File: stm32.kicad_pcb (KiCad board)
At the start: 4 copper layers, 50 x 100 mm, 108 parts, among them CN1 SM04B-SRSS-TB (LF)(SN), J3 B2B-PH-SM4-TB (LF)(SN), P1 TYPE-C 16PIN 2MD(073), Q1 DMG2301L-7, SW1 JS102011JCQN, U1 STM32L431KBU6_C2826408, U13 CH340C_C7464026, U2 MCP73833T-AMI/MF, U3 TPS631000DRLR, U4 OPT3004DNPR, U5 XC6206P332MR_C347376, U6 INA260AIPWR, U8 BME280

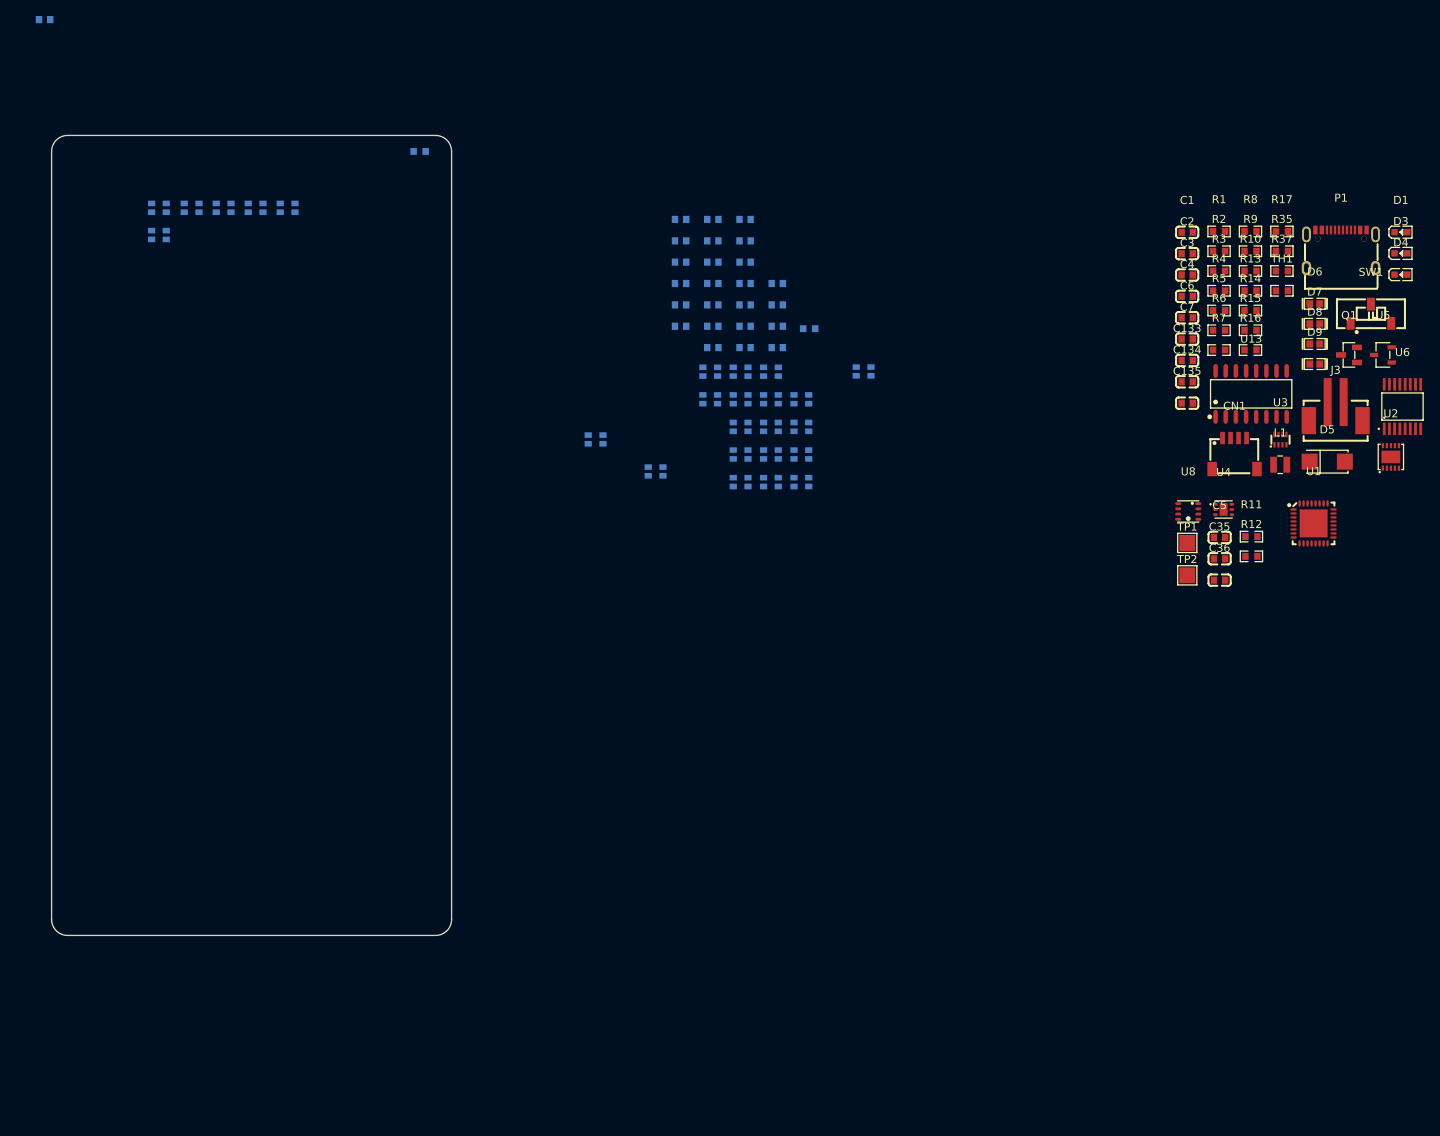
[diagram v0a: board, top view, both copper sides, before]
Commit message: Added pull up / pull down on mode pin tps
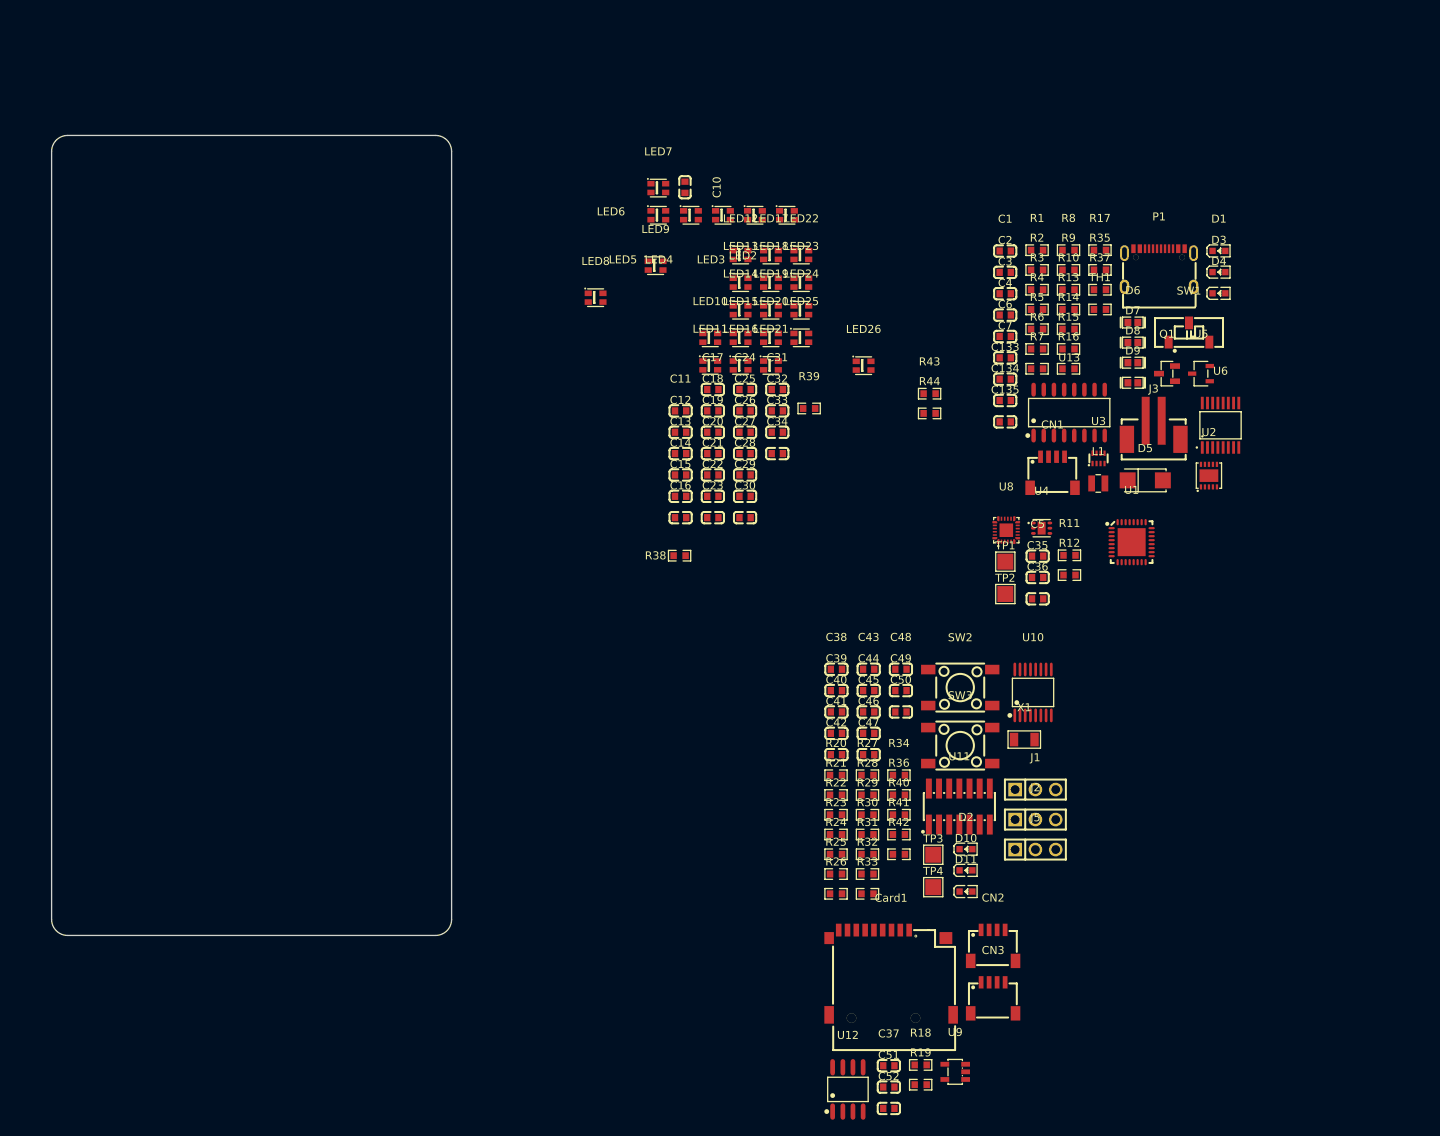
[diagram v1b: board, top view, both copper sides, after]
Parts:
- added C37: CC0603KRX7R9BB104, easyeda2kicad:C0603, F.Cu at (154.2, 150.3)
- added C38: CL10A475KO8NNNC, easyeda2kicad:C0603, F.Cu at (147.6, 100.7)
- added C39: CC0603KRX7R9BB104, easyeda2kicad:C0603, F.Cu at (147.6, 103.4)
- added C40: CC0603KRX7R9BB104, easyeda2kicad:C0603, F.Cu at (147.6, 106.1)
- added C41: CC0603KRX7R9BB104, easyeda2kicad:C0603, F.Cu at (147.6, 108.7)
- added C42: CL10A105KB8NNNC, easyeda2kicad:C0603, F.Cu at (147.6, 111.4)
- added C43: CL10A105KB8NNNC, easyeda2kicad:C0603, F.Cu at (151.6, 100.7)
- added C44: 0603CG7R0C500NT, easyeda2kicad:C0603, F.Cu at (151.6, 103.4)
- added C45: 0603CG7R0C500NT, easyeda2kicad:C0603, F.Cu at (151.6, 106.1)
- added C46: CC0603KRX7R9BB104, easyeda2kicad:C0603, F.Cu at (151.6, 108.7)
- added C47: CC0603KRX7R9BB104, easyeda2kicad:C0603, F.Cu at (151.6, 111.4)
- added C48: CC0603KRX7R9BB104, easyeda2kicad:C0603, F.Cu at (155.7, 100.7)
- added C49: CC0603KRX7R9BB104, easyeda2kicad:C0603, F.Cu at (155.7, 103.4)
- added C50: CC0603KRX7R9BB104, easyeda2kicad:C0603, F.Cu at (155.7, 106.1)
- added C51: CC0603KRX7R9BB104, easyeda2kicad:C0603, F.Cu at (154.2, 153.0)
- added C52: CC0603KRX7R9BB104, easyeda2kicad:C0603, F.Cu at (154.2, 155.6)
- added CN2: SM04B-SRSS-TB (LF)(SN), easyeda2kicad:CONN-SMD_4P-P1.00_SM04B-SRSS-TB-LF-SN, F.Cu at (167.2, 135.2)
- added CN3: SM04B-SRSS-TB (LF)(SN), easyeda2kicad:CONN-SMD_4P-P1.00_SM04B-SRSS-TB-LF-SN, F.Cu at (167.2, 141.8)
- added Card1: TF PUSH, easyeda2kicad:TF-SMD_TF-PUSH, F.Cu at (154.4, 138.6)
- added D10: KT-0603R, easyeda2kicad:LED0603-RD, F.Cu at (163.8, 125.9)
- added D11: KT-0603R, easyeda2kicad:LED0603-RD, F.Cu at (163.8, 128.5)
- added D2: 0603 Green 509-620mcd, easyeda2kicad:LED0603-RD, F.Cu at (163.8, 123.2)
- added J1: PZ254V-11-03P_C2937625, easyeda2kicad:HDR-TH_3P-P2.54-V-M, F.Cu at (172.5, 115.8)
- added J2: PZ254V-11-03P_C2937625, easyeda2kicad:HDR-TH_3P-P2.54-V-M, F.Cu at (172.5, 119.5)
- added J5: PZ254V-11-03P_C2937625, easyeda2kicad:HDR-TH_3P-P2.54-V-M, F.Cu at (172.5, 123.3)
- added R18: 0603WAF1002T5E, easyeda2kicad:R0603, F.Cu at (158.1, 150.2)
- added R19: 0603WAF1002T5E, easyeda2kicad:R0603, F.Cu at (158.1, 152.7)
- added R20: 0603WAF4701T5E, easyeda2kicad:R0603, F.Cu at (147.6, 114.0)
- added R21: 0603WAF1002T5E, easyeda2kicad:R0603, F.Cu at (147.6, 116.4)
- added R22: 0603WAF1000T5E, easyeda2kicad:R0603, F.Cu at (147.6, 118.9)
- added R23: 0603WAF1000T5E, easyeda2kicad:R0603, F.Cu at (147.6, 121.4)
- added R24: 0603WAF1000T5E, easyeda2kicad:R0603, F.Cu at (147.6, 123.9)
- added R25: 0603WAF220JT5E, easyeda2kicad:R0603, F.Cu at (147.6, 126.3)
- added R26: 0603WAF0000T5E, easyeda2kicad:R0603, F.Cu at (147.6, 128.8)
- added R27: 0603WAF0000T5E, easyeda2kicad:R0603, F.Cu at (151.5, 114.0)
- added R28: 0603WAF0000T5E, easyeda2kicad:R0603, F.Cu at (151.5, 116.4)
- added R29: 0603WAF0000T5E, easyeda2kicad:R0603, F.Cu at (151.5, 118.9)
- added R30: 0603WAF1002T5E, easyeda2kicad:R0603, F.Cu at (151.5, 121.4)
- added R31: 0603WAF1002T5E, easyeda2kicad:R0603, F.Cu at (151.5, 123.9)
- added R32: 0603WAF220JT5E, easyeda2kicad:R0603, F.Cu at (151.5, 126.3)
- added R33: 0603WAF220JT5E, easyeda2kicad:R0603, F.Cu at (151.5, 128.8)
- added R34: 0603WAF4701T5E, easyeda2kicad:R0603, F.Cu at (155.4, 114.0)
- added R36: 0603WAF1002T5E, easyeda2kicad:R0603, F.Cu at (155.4, 116.4)
- added R40: 0603WAF4701T5E, easyeda2kicad:R0603, F.Cu at (155.4, 118.9)
- added R41: 0603WAF1001T5E, easyeda2kicad:R0603, F.Cu at (155.4, 121.4)
- added R42: 0603WAF1000T5E, easyeda2kicad:R0603, F.Cu at (155.4, 123.9)
- added R43: 0603WAF1002T5E, easyeda2kicad:R0603, F.Cu at (159.2, 66.3)
- added R44: 0603WAF1002T5E, easyeda2kicad:R0603, F.Cu at (159.2, 68.8)
- added SW2: 6.0*6.0*6.0, easyeda2kicad:SW-SMD_4P-L6.0-W6.0-P4.50-LS8.6, F.Cu at (163.1, 103.0)
- added SW3: 6.0*6.0*6.0, easyeda2kicad:SW-SMD_4P-L6.0-W6.0-P4.50-LS8.6, F.Cu at (163.1, 110.3)
- added TP3: TestPoint, TestPoint:TestPoint_Pad_2.0x2.0mm, F.Cu at (159.7, 123.9)
- added TP4: TestPoint, TestPoint:TestPoint_Pad_2.0x2.0mm, F.Cu at (159.7, 128.0)
- added U10: MAX3221ECPWR, easyeda2kicad:TSSOP-16_L5.0-W4.4-P0.65-LS6.4-BL, F.Cu at (172.2, 103.6)
- added U11: HB-PH9-12727PB2GOB, easyeda2kicad:HDR-SMD_14P-P1.27-V-M-R2-C7-LS5.5, F.Cu at (163.0, 117.9)
- added U12: TMP75AIDR, easyeda2kicad:SOIC-8_L4.9-W3.9-P1.27-LS6.0-BL, F.Cu at (149.0, 153.2)
- added U9: SN74AHCT1G125DBVR, easyeda2kicad:SOT-23-5_L3.0-W1.7-P0.95-LS2.8-BR, F.Cu at (162.4, 151.1)
- added X1: SC-32S32.768kHz20PPM7pF, easyeda2kicad:OSC-SMD_L3.2-W1.5, F.Cu at (171.1, 109.5)
- C10, C11, C12, C13, C14, C15, C16, C17, C18, C19, C20, C21, C22, C23, C24, C25, C26, C27, C28, C29, C30, C31, C32, C33, C34, LED10, LED11, LED12, LED13, LED14, LED15, LED16, LED17, LED18, LED19, LED2, LED20, LED21, LED22, LED23, LED24, LED25, LED26, LED3, LED4, LED5, LED6, LED7, LED8, LED9, R38, R39: moved to F.Cu
- U8: value BME280 -> MPU6500; footprint easyeda2kicad:LGA-8_BME280_BL -> easyeda2kicad:QFN-24_L3.0-W3.0-P0.40-BL-EP
- moved C10 82.7 mm to (128.7, 40.5), turned to -90 degrees
- moved LED7 62.7 mm to (125.3, 40.6)
- moved LED6 62.4 mm to (125.3, 44.0)
- moved LED2 62.4 mm to (141.4, 44.0)
- moved LED3 62.4 mm to (137.4, 44.0)
- moved LED4 62.4 mm to (133.4, 44.0)
- moved LED5 62.4 mm to (129.4, 44.0)
- moved R38 60.1 mm to (128.0, 86.5)
- moved C16 37.3 mm to (128.1, 81.8)
- moved C23 37.3 mm to (132.2, 81.8)
- moved C30 37.3 mm to (136.2, 81.8)
- moved C15 31.9 mm to (128.1, 79.1)
- moved C22 31.9 mm to (132.2, 79.1)
- moved C29 31.9 mm to (136.2, 79.1)
- moved LED12 28.4 mm to (135.6, 48.9)
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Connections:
- net /USB/scl2 renamed /stm32_page/I2C3_SCL
- net /sensors/DIN renamed /sensors/led_matrix/DIN
- CN1 pad 3: /USB/sda2 -> /stm32_page/I2C3_SDA
- R17 pad 1: /USB/sda2 -> /stm32_page/I2C3_SDA
- U1 pad 1: unconnected-(U1-VDD-Pad1) -> +3V3
- U1 pad 10: unconnected-(U1-PA4-Pad10) -> /stm32_page/SD_CD
- U1 pad 11: unconnected-(U1-PA5-Pad11) -> /stm32_page/IMU_INT
- U1 pad 12: unconnected-(U1-PA6-Pad12) -> /stm32_page/SPI1_MISO
- U1 pad 13: unconnected-(U1-PA7-Pad13) -> /stm32_page/I2C3_SCL_R
- U1 pad 14: unconnected-(U1-PB0-Pad14) -> /stm32_page/LED1
- U1 pad 15: unconnected-(U1-PB1-Pad15) -> /stm32_page/LED2
- U1 pad 16: unconnected-(U1-VSS-Pad16) -> GND
- U1 pad 17: unconnected-(U1-VDD-Pad17) -> +3V3
- U1 pad 18: unconnected-(U1-PA8-Pad18) -> /stm32_page/PB_SW1
- U1 pad 19: unconnected-(U1-PA9-Pad19) -> /USB/TXD_0
- U1 pad 2: unconnected-(U1-PC14-OSC32_IN-Pad2) -> Net-(U1-PC14-OSC32_IN)
- U1 pad 20: unconnected-(U1-PA10-Pad20) -> /USB/RXD_0
- U1 pad 21: unconnected-(U1-PA11-Pad21) -> /stm32_page/PWM_CH4
- U1 pad 22: unconnected-(U1-PA12-Pad22) -> /stm32_page/SPI1_MOSI
- U1 pad 23: unconnected-(U1-PA13-Pad23) -> /stm32_page/SWDIO
- U1 pad 24: unconnected-(U1-PA14-Pad24) -> /stm32_page/SWCLK
- U1 pad 25: unconnected-(U1-PA15-Pad25) -> /stm32_page/PWM_CH1
- U1 pad 26: unconnected-(U1-PB3-Pad26) -> /stm32_page/LED3
- U1 pad 27: unconnected-(U1-PB4-Pad27) -> /stm32_page/I2C3_SDA
- U1 pad 28: unconnected-(U1-PB5-Pad28) -> /stm32_page/RGB_LEDS
- U1 pad 29: unconnected-(U1-PB6-Pad29) -> /stm32_page/I2C1_SCL_R
- U1 pad 3: unconnected-(U1-PC15-OSC32_OUT-Pad3) -> Net-(U1-PC15-OSC32_OUT)
- U1 pad 30: unconnected-(U1-PB7-Pad30) -> /sensors/SDA
- U1 pad 31: unconnected-(U1-PH3/BOOT0-Pad31) -> /stm32_page/BOOT0
- U1 pad 32: unconnected-(U1-VSS-Pad32) -> GND
- U1 pad 33: unconnected-(U1-EP-Pad33) -> GND
- U1 pad 4: unconnected-(U1-NRST-Pad4) -> /stm32_page/STM32_NRST
- U1 pad 5: unconnected-(U1-VDDA/VREF+-Pad5) -> +3V3
- U1 pad 6: unconnected-(U1-PA0/CK_IN-Pad6) -> /stm32_page/SYS_WKUP1
- U1 pad 7: unconnected-(U1-PA1-Pad7) -> /stm32_page/SPI1_SCK
- U1 pad 8: unconnected-(U1-PA2-Pad8) -> /stm32_page/UART2_TX
- U1 pad 9: unconnected-(U1-PA3-Pad9) -> /stm32_page/UART2_RX
- U3 pad 6: P_MODE -> /USB/P_MODE
- U4 pad 5: /sensors/INT_L -> /stm32_page/SYS_WKUP1
- U6 pad 8: /USB/sda2 -> /stm32_page/I2C3_SDA
- U8 pad 1: GND -> unconnected-(U8-NC-Pad1)
- U8 pad 2: +3V3 -> unconnected-(U8-NC-Pad2)
- U8 pad 3: /sensors/SDA -> unconnected-(U8-NC-Pad3)
- U8 pad 4: /sensors/SCL -> unconnected-(U8-NC-Pad4)
- U8 pad 5: GND -> unconnected-(U8-NC-Pad5)
- U8 pad 6: +3V3 -> unconnected-(U8-NC-Pad6)
- U8 pad 7: GND -> unconnected-(U8-AUX_CL-Pad7)

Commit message: Added missing filter caps on ina260
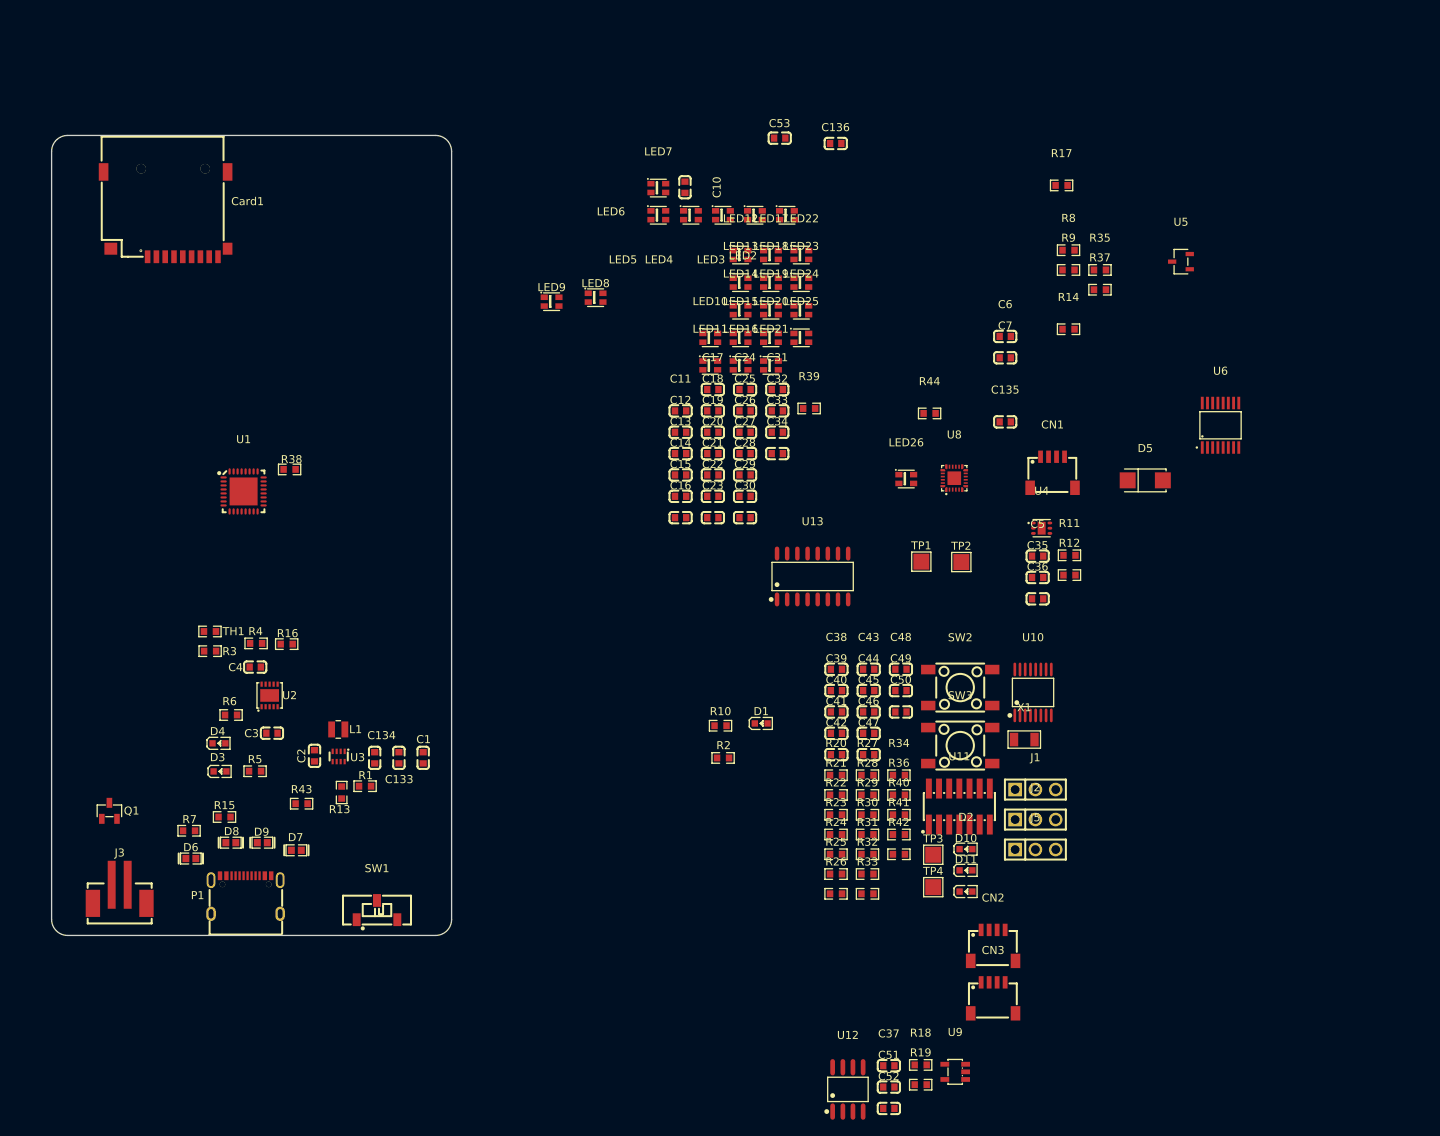
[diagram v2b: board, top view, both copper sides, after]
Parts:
- added C136: CL10A106KP8NNNC, easyeda2kicad:C0603, F.Cu at (147.5, 35.0)
- added C53: CC0603KRX7R9BB104, easyeda2kicad:C0603, F.Cu at (140.5, 34.3)
- moved Q1 143.1 mm to (56.7, 118.4), turned to -90 degrees
- moved J3 141.7 mm to (58.0, 128.8)
- moved D3 139.6 mm to (70.5, 113.5)
- moved P1 138.5 mm to (73.8, 128.9)
- moved D4 137.1 mm to (70.4, 110.0)
- moved D6 135.5 mm to (66.9, 124.4)
- moved Card1 131.2 mm to (63.8, 43.9), turned to 180 degrees
- moved D8 127.7 mm to (71.9, 122.4)
- moved SW1 124.6 mm to (90.2, 130.8)
- moved D9 123.1 mm to (75.8, 122.4), turned to 180 degrees
- moved D7 122.3 mm to (80.1, 123.4), turned to 180 degrees
- moved R7 120.7 mm to (66.7, 120.9)
- moved R15 120.6 mm to (71.1, 119.2)
- moved U2 120.6 mm to (76.8, 104.0)
- moved TH1 118.3 mm to (69.3, 96.0)
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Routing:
- added copper zone on In1.Cu, net GND
- added copper zone on In2.Cu, net GND

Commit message: Advanced placement , minor schem changes
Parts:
- removed R26, R27: 0603WAF0000T5E, easyeda2kicad:R0603
- removed TP3, TP4: TestPoint, TestPoint:TestPoint_Pad_2.0x2.0mm
- C10, C11, C12, C13, C14, C15, C16, C17, C18, C19, C20, C21, C22, C23, C24, C25, C26, C27, C28, C29, C30, C31, C32, C33, C34, C44, C45, D5, R28, R29, X1: moved to B.Cu
- moved R35 125.7 mm to (66.0, 102.5)
- moved R37 125.5 mm to (66.0, 104.5)
- moved J1 125.2 mm to (52.5, 80.0), turned to 90 degrees
- moved J2 123.4 mm to (52.5, 90.5), turned to -90 degrees
- moved D5 122.6 mm to (71.3, 119.9), turned to -90 degrees
- moved C5 122.5 mm to (52.8, 61.8), turned to 90 degrees
- moved J5 122.2 mm to (52.5, 100.0), turned to -90 degrees
- moved U9 120.3 mm to (65.1, 80.3), turned to -90 degrees
- moved R12 120.1 mm to (58.6, 67.3)
- moved R11 119.7 mm to (60.2, 59.2)
- moved U5 119.6 mm to (84.1, 104.0), turned to 180 degrees
- moved U4 118.8 mm to (56.4, 61.8)
- moved U6 109.6 mm to (93.2, 109.2)
- moved SW3 108.8 mm to (80.0, 40.0)
- moved C35 108.2 mm to (64.6, 86.3), turned to -90 degrees
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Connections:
- C10 pad 1: GND -> /stm32_page/UART2_RX
- C11 pad 1: GND -> /stm32_page/UART2_RX
- C12 pad 1: GND -> /stm32_page/UART2_RX
- C13 pad 1: GND -> /stm32_page/UART2_RX
- C14 pad 1: GND -> /stm32_page/UART2_RX
- C15 pad 1: GND -> /stm32_page/UART2_RX
- C16 pad 1: GND -> /stm32_page/UART2_RX
- C17 pad 1: GND -> /stm32_page/UART2_RX
- C18 pad 1: GND -> /stm32_page/UART2_RX
- C19 pad 1: GND -> /stm32_page/UART2_RX
- C20 pad 1: GND -> /stm32_page/UART2_RX
- C21 pad 1: GND -> /stm32_page/UART2_RX
- C22 pad 1: GND -> /stm32_page/UART2_RX
- C23 pad 1: GND -> /stm32_page/UART2_RX
- C24 pad 1: GND -> /stm32_page/UART2_RX
- C25 pad 1: GND -> /stm32_page/UART2_RX
- C26 pad 1: GND -> /stm32_page/UART2_RX
- C27 pad 1: GND -> /stm32_page/UART2_RX
- C28 pad 1: GND -> /stm32_page/UART2_RX
- C29 pad 1: GND -> /stm32_page/UART2_RX
- C30 pad 1: GND -> /stm32_page/UART2_RX
- C31 pad 1: GND -> /stm32_page/UART2_RX
- C32 pad 1: GND -> /stm32_page/UART2_RX
- C33 pad 1: GND -> /stm32_page/UART2_RX
- C34 pad 1: GND -> /stm32_page/UART2_RX
- C44 pad 1: GND -> /stm32_page/UART2_RX
- C45 pad 1: GND -> /stm32_page/UART2_RX
- C49 pad 1: GND -> /stm32_page/UART2_RX
- D3 pad 1: /USB/STAT2 -> Net-(D3-K)
- D3 pad 2: Net-(D3-A) -> +5VP
- D4 pad 1: /USB/STAT1 -> Net-(D4-K)
- D4 pad 2: Net-(D4-A) -> +5VP
- J3 pad 1: GND -> /stm32_page/UART2_RX
- J5 pad 3: GND -> /stm32_page/UART2_RX
- LED10 pad 2: GND -> /stm32_page/UART2_RX
- LED11 pad 2: GND -> /stm32_page/UART2_RX
- LED12 pad 2: GND -> /stm32_page/UART2_RX
- LED13 pad 2: GND -> /stm32_page/UART2_RX
- LED14 pad 2: GND -> /stm32_page/UART2_RX
- LED15 pad 2: GND -> /stm32_page/UART2_RX
- LED16 pad 2: GND -> /stm32_page/UART2_RX
- LED17 pad 2: GND -> /stm32_page/UART2_RX
- LED18 pad 2: GND -> /stm32_page/UART2_RX
- LED19 pad 2: GND -> /stm32_page/UART2_RX
- LED2 pad 2: GND -> /stm32_page/UART2_RX
- LED20 pad 2: GND -> /stm32_page/UART2_RX
- LED21 pad 2: GND -> /stm32_page/UART2_RX
- LED22 pad 2: GND -> /stm32_page/UART2_RX
- LED23 pad 2: GND -> /stm32_page/UART2_RX
- LED24 pad 2: GND -> /stm32_page/UART2_RX
- LED25 pad 2: GND -> /stm32_page/UART2_RX
- LED26 pad 2: GND -> /stm32_page/UART2_RX
- LED3 pad 2: GND -> /stm32_page/UART2_RX
- LED4 pad 2: GND -> /stm32_page/UART2_RX
- LED5 pad 2: GND -> /stm32_page/UART2_RX
- LED6 pad 2: GND -> /stm32_page/UART2_RX
- LED7 pad 2: GND -> /stm32_page/UART2_RX
- LED8 pad 2: GND -> /stm32_page/UART2_RX
- LED9 pad 2: GND -> /stm32_page/UART2_RX
- P1 pad 13: GND -> /stm32_page/UART2_RX
- P1 pad 14: GND -> /stm32_page/UART2_RX
- R36 pad 2: GND -> /stm32_page/UART2_RX
- R5 pad 1: Net-(D3-A) -> /USB/STAT2
- R5 pad 2: +5VP -> Net-(D3-K)
- R6 pad 1: Net-(D4-A) -> /USB/STAT1
- R6 pad 2: +5VP -> Net-(D4-K)
- U1 pad 10: /stm32_page/SD_CD -> /stm32_page/UART2_RX
- U10 pad 14: GND -> /stm32_page/UART2_RX
- U8 pad 9: GND -> /stm32_page/UART2_RX
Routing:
- net +5V: track 0.00 -> 105.9 mm, vias 0 -> 15
- net /stm32_page/UART2_RX: track 0.00 -> 81.4 mm, vias 0 -> 62
- net /stm32_page/IMU_INT: track 0.00 -> 37.1 mm
- net /stm32_page/UART2_TX_CONN: track 0.00 -> 30.8 mm
- net /stm32_page/MAX3221_TX_IN: track 0.00 -> 22.0 mm
- net LIPO+: track 0.00 -> 21.6 mm
- net /stm32_page/MAX3221_RX_OUT: track 0.00 -> 20.3 mm
- net /USB/raw_voltage: track 0.00 -> 11.7 mm, vias 0 -> 1
- net /stm32_page/UART2_RX_CONN: track 0.00 -> 10.9 mm
- net +3V3: track 0.00 -> 8.66 mm, vias 0 -> 1
- net /stm32_page/OSC32_IN: track 0.00 -> 6.98 mm
- net /stm32_page/OSC32_OUT: track 0.00 -> 6.84 mm
- net Net-(U1-PC15-OSC32_OUT): track 0.00 -> 6.48 mm, vias 0 -> 1
- net Net-(U1-PC14-OSC32_IN): track 0.00 -> 6.03 mm, vias 0 -> 1
- net Net-(LED16-DO): track 0.00 -> 5.93 mm
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- added copper zone on F.Cu, net +5VP
